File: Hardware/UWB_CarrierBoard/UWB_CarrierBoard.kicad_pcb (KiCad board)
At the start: 2 copper layers, 43.8 x 37.5 mm, 14 parts, among them J1 Conn_01x09_Socket, J2 Conn_01x09_Socket, U1 DWM1000

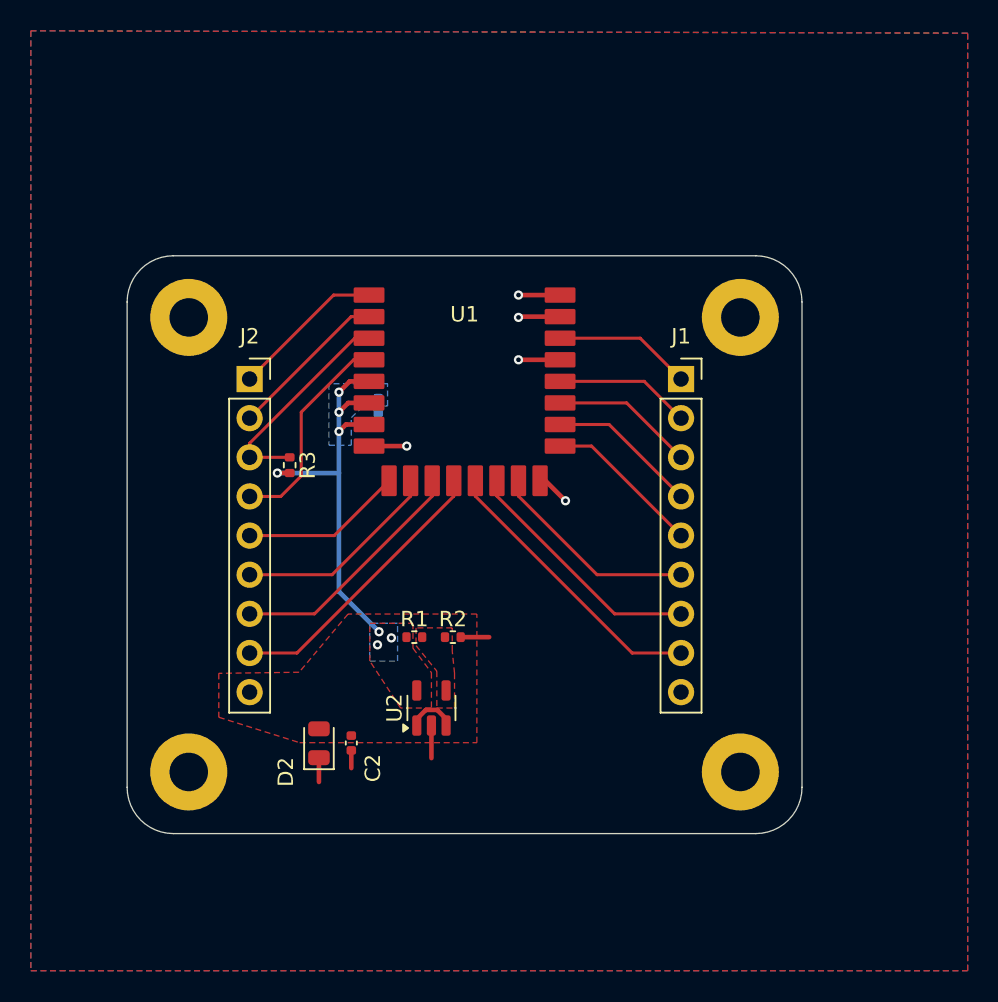
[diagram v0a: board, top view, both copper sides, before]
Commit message: Finished up the board, generated gerbers, and all other stuffs.
- Added datasheets
- Changed the TVS diode to smth JLC had in stock
- Added pin labels
- Obviously regenerated the gerbers n related stuff
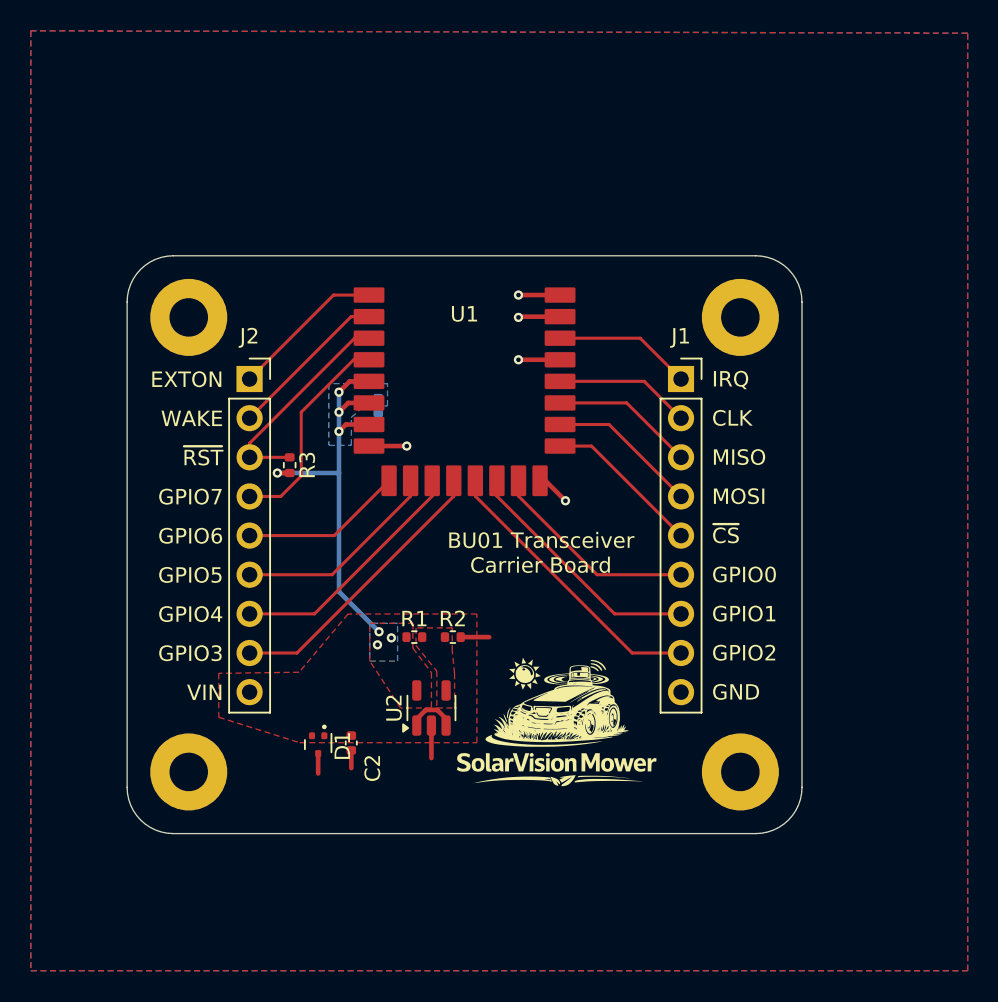
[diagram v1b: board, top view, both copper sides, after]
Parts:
- removed D2: D_TVS, Diode_SMD:D_0805_2012Metric
- added D1: D_TVS, Package_TO_SOT_SMD:SOT-723, F.Cu at (164.3, 74.9)
- added G***: LOGO, Footprints:SolarVisionMowerLogo, F.Cu at (179.9, 73.5)
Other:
- board text added: "CLK"
- board text added: "EXTON"
- board text added: "GND"
- board text added: "GPIO0"
- board text added: "GPIO1"
- board text added: "GPIO2"
- board text added: "GPIO3"
- board text added: "GPIO4"
- board text added: "GPIO5"
- board text added: "GPIO6"
- board text added: "GPIO7"
- board text added: "IRQ"
- board text added: "MISO"
- board text added: "MOSI"
- board text added: "VIN"
- board text added: "WAKE"
- board text added: "~{CS}"
- board text added: "~{RST}"
